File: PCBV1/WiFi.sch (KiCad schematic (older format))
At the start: 0 parts

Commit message: Made comments and some circuits.
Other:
- note added: "Wi-Fi module & antenna.\n\nProposed ICs:\n\nNXP 88W8987\nMaxim MAX2831ETM+"
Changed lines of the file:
@@
 $Descr A4 11693 8268
 encoding utf-8
-Sheet 4 9
+Sheet 3 8
 Title "Smart Mirror"
 Date "2021-01-21"
@@
 Comment4 ""
 $EndDescr
+Text Notes 4900 3550 0    50   ~ 0
+Wi-Fi module & antenna.\n\nProposed ICs:\n\nNXP 88W8987\nMaxim MAX2831ETM+
 $EndSCHEMATC

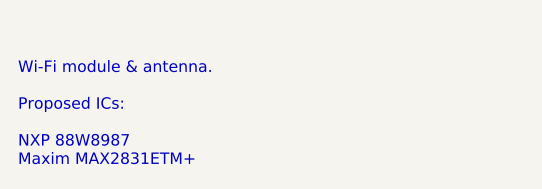
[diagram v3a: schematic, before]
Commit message: Added NAND flash with connections, updated IO config.
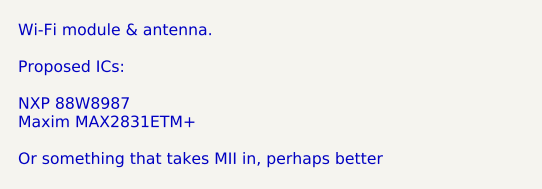
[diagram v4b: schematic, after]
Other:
- note added: "Wi-Fi module & antenna.\n\nProposed ICs:\n\nNXP 88W8987\nMaxim MAX2831ETM+\n\nOr something that takes MII in, perhaps better"
- note removed: "Wi-Fi module & antenna.\n\nProposed ICs:\n\nNXP 88W8987\nMaxim MAX2831ETM+"
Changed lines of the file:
@@
 $EndDescr
 Text Notes 4900 3550 0    50   ~ 0
-Wi-Fi module & antenna.\n\nProposed ICs:\n\nNXP 88W8987\nMaxim MAX2831ETM+
+Wi-Fi module & antenna.\n\nProposed ICs:\n\nNXP 88W8987\nMaxim MAX2831ETM+\n\nOr something that takes MII in, perhaps better
 $EndSCHEMATC

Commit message: Laid final hands on Wi-Fi and all circuits. Started work on PCB.
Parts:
- added AE1: Inverted-F Antenna, RF_Antenna:Texas_SWRA117D_2.4GHz_Left, symbol Device:Antenna_Shield
- added C10: 0.8p, Capacitor_SMD:C_0402_1005Metric, symbol Device:C
- added C11, C12: NM, Capacitor_SMD:C_0402_1005Metric, symbol Device:C
- added C13, C14: 12p, Capacitor_SMD:C_0603_1608Metric, symbol Device:C
- added C15, C16: 47n, Capacitor_SMD:C_0603_1608Metric, symbol Device:C
- added C17, C18, C5, C7: 10u, Capacitor_SMD:C_0603_1608Metric, symbol Device:C
- added C4, C6: 100n, Capacitor_SMD:C_0603_1608Metric, symbol Device:C
- added C8: 10n, Capacitor_SMD:C_0603_1608Metric, symbol Device:C
- added C9: 1.8p, Capacitor_SMD:C_0402_1005Metric, symbol Device:C
- added FB1, FB2: 600R, Inductor_SMD:L_0603_1608Metric, symbol Device:Ferrite_Bead_Small
- added L1: 2.7n, Inductor_SMD:L_0402_1005Metric, symbol Device:L
- added L2: 0, Inductor_SMD:L_0402_1005Metric, symbol Device:L
- added R10, R11, R12, R7, R8, R9: 33, Resistor_SMD:R_0603_1608Metric, symbol Device:R
- added R13: 50, Resistor_SMD:R_0603_1608Metric, symbol Device:R
- added R2, R3, R4, R5, R6: 82k, Resistor_SMD:R_0603_1608Metric, symbol Device:R
- added U5: MCP112T-315E_LB, Personal_ICs:MCP112T-315E-LB, symbol Personal_ICs:MCP112T-315E_LB
- added U6: WF200D, Personal_ICs:WF200D, symbol Personal_ICs:WF200D
- added Y1: ECS-384-10-33B-CKY-TR, Personal_Actives:ECS3841033BCKYTR, symbol Device:Crystal_GND24_Small
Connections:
- new net: R13.1, U6.12 (RF_2)
- new net: C14.1, C16.1, C18.1, FB2.1, U6.13 (VDD_PA)
- new net: R12.2, U6.26 (SDIO_CLK/_SPI_CLK)
- new net: R11.2, U6.27 (SDIO_CMD/_SPI_MOSI)
- new net: R10.2, U6.28 (SDIO_DAT0/_SPI_MISO)
- new net: R9.2, U6.29 (SDIO_DAT1_/_SPI_WIRQ)
- new net: R8.2, U6.30 (SDIO_DAT2/_HIF_SEL)
- new net: R7.2, U6.31 (SDIO_DAT3/_SPI_CSN)
- new net: U6.7 (XTAL_I), Y1.1
- new net: U6.8 (XTAL_O), Y1.3
- new net: C13.1, C15.1, C17.1, FB1.1, U6.9 (VDD_RF)
- new net: C10.1, C11.1, L1.2, L2.1
- new net: AE1.1 (A), C12.1, L2.2
- new net +3V3: C4.1, C5.1, C6.1, C7.2, C8.2, FB1.2, FB2.2, R2.1, R3.1, R4.1, R5.1, R6.1, U5.3 (VDD), U6.25 (VDD_DIG), U6.32 (VDD_IO)
- new net GND: AE1.2 (Shield), C10.2, C11.2, C12.2, C13.2, C14.2, C15.2, C16.2, C17.2, C18.2, C4.2, C5.2, C6.2, C7.1, C8.1, C9.2, R13.2, U5.2 (VSS), U6.10 (GND_1), U6.14 (RESERVE_1), U6.23 (GPIO/LP_CLK), U6.33 (GND_2), Y1.2, Y1.4
- new net RESET: U5.1 (VOUT), U6.15 (RESETN)
- new net RF_O: C9.1, L1.1, U6.11 (RF_1)
- new net SDIO_CLK: R12.1
- new net SDIO_CMD: R11.1, R6.2
- new net SDIO_DATA0: R10.1, R5.2
- new net SDIO_DATA1: R4.2, R9.1
- new net SDIO_DATA2: R3.2, R8.1
- new net SDIO_DATA3: R2.2, R7.1
- no-connect marks 0 -> 14
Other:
- note added: "50 Ohm antenna impedance matching"
- note added: "Antenna input impedance matching"
- note added: "RF output impedance matching"
- note added: "Voltage monitor"
- note removed: "Wi-Fi module & antenna.\n\nProposed ICs:\n\nNXP 88W8987\nMaxim MAX2831ETM+\n\nOr something that takes MII in, perhaps better"
